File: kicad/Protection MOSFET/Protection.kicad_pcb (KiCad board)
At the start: 2 copper layers, 50 x 80 mm, 64 parts, among them P1 VI2, P2 LED, P3 VO2, P4 VI1, P5 VAC2, P6 VO1, P7 Taster, Q1 BC858, Q2 Q_NMOS_GDS, Q3 BC850, Q4 BC850, Q5 BC850, Q6 BC858, Q7 BC850, Q8 Q_NMOS_GDS, Q9 BC850, U1 LM319, U2 LTV-817

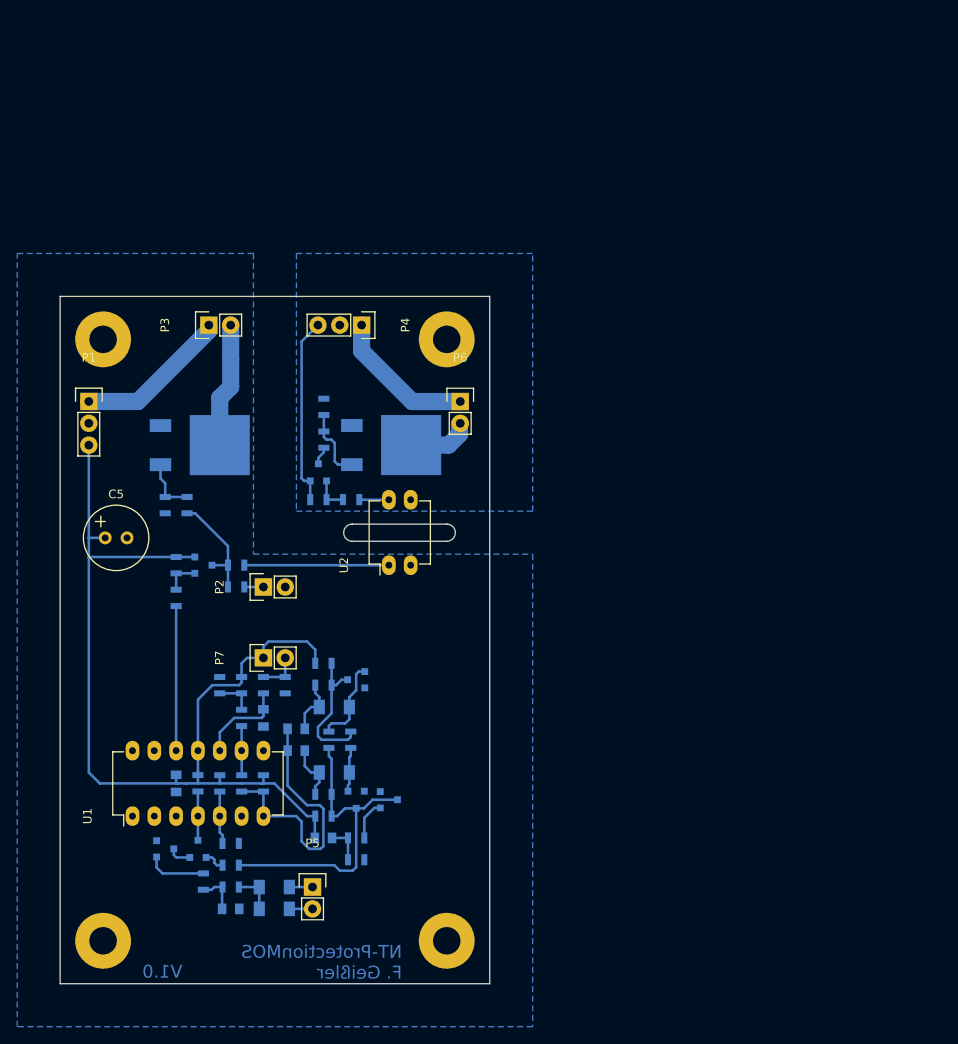
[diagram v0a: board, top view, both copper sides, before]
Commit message: Corrected MOSFET Protection board
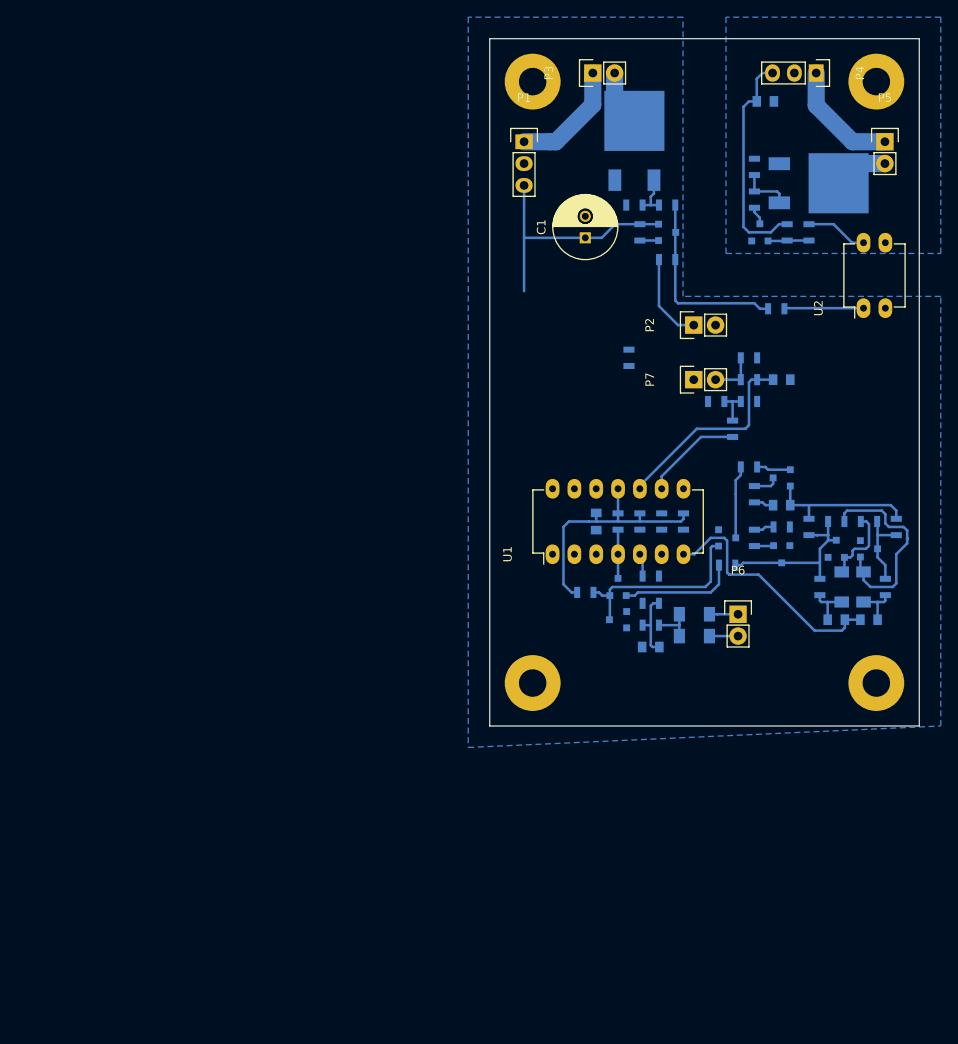
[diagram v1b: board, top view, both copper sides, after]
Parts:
- removed the REF** at (55.0, 125.0)
- removed the REF** at (95.0, 125.0)
- removed the REF** at (95.0, 55.0)
- removed the REF** at (55.0, 55.0)
- added C8: 1u, Capacitors_SMD:C_0805, B.Cu at (134.0, 59.7)
- added Q10: BC850, TO_SOT_Packages_SMD:SOT-23, B.Cu at (140.3, 79.4)
- added Q11: BC850, TO_SOT_Packages_SMD:SOT-23, B.Cu at (144.1, 79.4)
- added R32: 10k, Resistors_SMD:R_0805, B.Cu at (147.3, 76.8)
- added R33: 4k7, Resistors_SMD:R_0805, B.Cu at (130.2, 57.1)
- added R34: 47k, Resistors_SMD:R_0805, B.Cu at (146.1, 83.8)
- added REF**: Hole_M3, Mechanical:Hole_M3, F.Cu at (105.0, 95.0)
- added REF**: Hole_M3, Mechanical:Hole_M3, F.Cu at (145.0, 95.0)
- added REF**: Hole_M3, Mechanical:Hole_M3, F.Cu at (145.0, 25.0)
- added REF**: Hole_M3, Mechanical:Hole_M3, F.Cu at (105.0, 25.0)
- C1: value 15n -> 22u; footprint Capacitors_SMD:C_0805 -> Capacitors_ThroughHole:C_Radial_D7.5_L11.2_P2.5; moved to F.Cu
- C4: value 100n -> 15n
- C5: value 22u -> 100n; footprint Capacitors_Elko_ThroughHole:Elko_vert_11.2x7.5mm_RM2.5_CopperClear -> Capacitors_SMD:C_0805; moved to B.Cu
- C7: value 1u -> 100n
- P5: value VAC2 -> VO1
- P6: value VO1 -> VAC2
- Q1, Q3, Q4, Q9: footprint Housings_SOT-23_SOT-143_TSOT-6:SOT-23 -> TO_SOT_Packages_SMD:SOT-23
- Q2: footprint Transistors_SMD:sot428 -> TO_SOT_Packages_SMD:SOT-428
- Q5: value BC850 -> BC858; footprint Housings_SOT-23_SOT-143_TSOT-6:SOT-23 -> TO_SOT_Packages_SMD:SOT-23
- Q6: value BC858 -> BC850; footprint Housings_SOT-23_SOT-143_TSOT-6:SOT-23 -> TO_SOT_Packages_SMD:SOT-23
- Q7: value BC850 -> Q_NMOS_GDS; footprint Housings_SOT-23_SOT-143_TSOT-6:SOT-23 -> TO_SOT_Packages_SMD:SOT-428
- Q8: value Q_NMOS_GDS -> BC856; footprint Transistors_SMD:sot428 -> TO_SOT_Packages_SMD:SOT-23
- R10: value 47k -> 22k
- R11: value 2k2 -> 10k
- R12: value 100k -> 22k
- R13, R19, R2: value 22k -> 10k
- R14: value 10k -> 100
- R17: value 22k -> 1k
- R18: value 100 -> 100k
- R21: value 22k -> 47k
- R22: value 22k -> 120k
- R23, R25, R3, R30: value 10k -> 22k
- R24: value 47k -> 10k
- R26: value 120k -> 22k
- R31: value 4k7 -> 10k
- R4: value 22k -> 100
- R5: value 100 -> 22k
- R9: value 22k -> 2k2
- moved P5 109.4 mm to (146.0, 32.0)
- moved R15 103.6 mm to (130.8, 34.9), turned to 90 degrees
- moved C3 93.2 mm to (132.1, 27.3), turned to 180 degrees
- moved R9 90.7 mm to (133.3, 51.4), turned to 180 degrees
- moved R12 90.1 mm to (137.2, 42.5), turned to 270 degrees
- moved Q7 89.0 mm to (137.2, 36.8), turned to 90 degrees
- moved R14 87.6 mm to (130.8, 38.7), turned to 90 degrees
- moved C6 79.2 mm to (140.3, 87.6), turned to 180 degrees
- moved Q5 78.9 mm to (131.4, 42.5), turned to 180 degrees
- moved C1 76.2 mm to (111.1, 43.2), turned to 90 degrees
- moved R26 75.6 mm to (140.3, 76.2), turned to 180 degrees
- moved R11 74.9 mm to (134.6, 42.5), turned to 90 degrees
- moved D1 74.7 mm to (141.0, 83.8), turned to 90 degrees
- moved R4 73.2 mm to (120.7, 39.4), turned to 180 degrees
- moved R30 73.0 mm to (144.1, 76.2), turned to 180 degrees
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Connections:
- C1 pad 1: Net-(C1-Pad1) -> V+
- C1 pad 2: V+ -> V-
- C2 pad 2: Net-(C2-Pad2) -> V+
- C3 pad 1: Net-(C3-Pad1) -> /V-1
- C3 pad 2: Net-(C3-Pad2) -> /V+1
- C4 pad 1: Net-(C3-Pad1) -> Net-(C4-Pad1)
- C4 pad 2: Net-(C4-Pad2) -> V+
- C5 pad 1: V+ -> V-
- C5 pad 2: V- -> Net-(C5-Pad2)
- C6 pad 1: V- -> /BTN
- C6 pad 2: V+ -> Net-(C6-Pad2)
- C7 pad 1: V- -> Net-(C7-Pad1)
- C7 pad 2: Net-(C7-Pad2) -> /BTN
- D1 pad 1: Net-(D1-Pad1) -> Net-(C6-Pad2)
- D2 pad 1: Net-(D1-Pad1) -> Net-(D2-Pad1)
- D3 pad 1: Net-(C3-Pad2) -> Net-(D2-Pad1)
- D4 pad 1: Net-(C4-Pad2) -> Net-(C7-Pad1)
- P5 pad 1: Net-(D1-Pad2) -> Net-(P4-Pad1)
- P5 pad 2: Net-(D2-Pad2) -> Net-(P5-Pad2)
- P6 pad 1: Net-(P4-Pad1) -> Net-(D2-Pad2)
- P6 pad 2: Net-(P6-Pad2) -> Net-(D3-Pad2)
- Q3 pad 2: Net-(Q3-Pad2) -> /STARTUP_FB
- Q4 pad 1: Net-(Q4-Pad1) -> /MAINS_DET
- Q4 pad 3: Net-(Q3-Pad2) -> /STARTUP_FB
- Q5 pad 2: V- -> /V+1
- Q6 pad 1: Net-(Q6-Pad1) -> /STARTUP_FB
- Q6 pad 2: /V+1 -> V-
- Q7 pad 1: Net-(D3-Pad2) -> Net-(Q7-Pad1)
- Q7 pad 2: V- -> Net-(P5-Pad2)
- Q7 pad 3: Net-(Q5-Pad3) -> /V-1
- Q8 pad 2: Net-(P6-Pad2) -> V+
- Q8 pad 3: /V-1 -> Net-(Q8-Pad3)
- Q9 pad 1: Net-(D4-Pad2) -> Net-(Q9-Pad1)
- Q9 pad 3: Net-(Q9-Pad3) -> /FF_STARTUP
- R10 pad 1: Net-(C3-Pad2) -> Net-(Q3-Pad1)
- R10 pad 2: Net-(Q5-Pad3) -> /FF_STARTUP
- R11 pad 1: Net-(R11-Pad1) -> Net-(Q5-Pad1)
- R11 pad 2: /ON -> /V+1
- R12 pad 1: Net-(C1-Pad1) -> Net-(R12-Pad1)
- R12 pad 2: V- -> Net-(Q5-Pad1)
- R13 pad 1: Net-(C2-Pad2) -> /STARTUP_FB
- R13 pad 2: Net-(Q4-Pad1) -> V+
- R14 pad 1: Net-(C1-Pad1) -> Net-(Q5-Pad3)
- R14 pad 2: Net-(Q5-Pad1) -> Net-(Q7-Pad1)
- R15 pad 1: Net-(D1-Pad1) -> Net-(Q7-Pad1)
- R15 pad 2: Net-(C2-Pad2) -> /V-1
- R16 pad 1: Net-(Q6-Pad1) -> Net-(Q6-Pad3)
- R16 pad 2: /V+1 -> Net-(Q8-Pad1)
- R17 pad 1: Net-(R17-Pad1) -> Net-(Q8-Pad3)
- R17 pad 2: Net-(Q6-Pad1) -> Net-(C4-Pad1)
- R18 pad 1: Net-(Q6-Pad3) -> Net-(C4-Pad1)
- R18 pad 2: Net-(Q8-Pad1) -> V-
- R19 pad 1: Net-(Q8-Pad1) -> Net-(C4-Pad1)
- R19 pad 2: /V-1 -> Net-(Q9-Pad1)
- R2 pad 1: V- -> Net-(Q1-Pad1)
- R2 pad 2: Net-(Q2-Pad1) -> V+
- R20 pad 1: V+ -> /BTN
- R20 pad 2: Net-(Q5-Pad3) -> V+
- R21 pad 1: Net-(D4-Pad2) -> Net-(C6-Pad2)
- R21 pad 2: Net-(Q5-Pad3) -> /FF_STARTUP
- R22 pad 1: Net-(Q9-Pad3) -> Net-(R22-Pad1)
- R22 pad 2: Net-(D3-Pad2) -> /BTN
- R23 pad 1: V+ -> Net-(C5-Pad2)
- R23 pad 2: Net-(Q9-Pad3) -> /MAINS_DET
- R24 pad 1: Net-(C4-Pad2) -> V+
- R24 pad 2: Net-(Q9-Pad3) -> /FF_STARTUP
- R25 pad 1: Net-(C3-Pad1) -> Net-(D2-Pad1)
- R25 pad 2: V+ -> Net-(C5-Pad2)
- R26 pad 1: Net-(R26-Pad1) -> Net-(D4-Pad2)
- R26 pad 2: Net-(C3-Pad1) -> /FF_STARTUP
- R27 pad 2: Net-(R26-Pad1) -> Net-(R22-Pad1)
- R3 pad 1: Net-(Q1-Pad1) -> Net-(R3-Pad1)
- R3 pad 2: V+ -> Net-(Q1-Pad1)
- R30 pad 1: Net-(P7-Pad2) -> Net-(Q11-Pad3)
- R30 pad 2: Net-(C7-Pad2) -> Net-(D1-Pad2)
- R31 pad 1: V- -> Net-(P7-Pad2)
- R31 pad 2: Net-(P7-Pad2) -> Net-(C8-Pad2)
- R4 pad 1: Net-(R4-Pad1) -> /ON
- R4 pad 2: Net-(Q1-Pad1) -> Net-(Q2-Pad1)
- R5 pad 2: /ON -> V-
- R9 pad 1: Net-(Q3-Pad1) -> Net-(R9-Pad1)
- R9 pad 2: Net-(Q5-Pad3) -> /ON
- U1 pad 10: Net-(C7-Pad2) -> Net-(C8-Pad2)
- U1 pad 12: Net-(R4-Pad1) -> Net-(R3-Pad1)
- U1 pad 7: Net-(C3-Pad1) -> /BTN
- U1 pad 9: Net-(R26-Pad1) -> Net-(R22-Pad1)
- U2 pad 1: Net-(R11-Pad1) -> Net-(R9-Pad1)
- U2 pad 4: Net-(R17-Pad1) -> Net-(R12-Pad1)
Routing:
- net V+: track 117.3 -> 75.4 mm
- net Net-(Q5-Pad3): track 37.5 -> 2.12 mm
- net Net-(C3-Pad1): track 31.7 -> 0.00 mm
- net /BTN: track 0.00 -> 29.1 mm
- net Net-(C8-Pad2): track 0.00 -> 23.9 mm
- net /STARTUP_FB: track 0.00 -> 22.6 mm
- net /FF_STARTUP: track 0.00 -> 20.2 mm
- net Net-(R4-Pad1): track 16.8 -> 0.00 mm
- net Net-(R11-Pad1): track 16.8 -> 0.00 mm
- net Net-(Q9-Pad3): track 16.0 -> 0.00 mm
- net Net-(D4-Pad2): track 10.1 -> 24.0 mm
- net Net-(R22-Pad1): track 0.00 -> 11.6 mm
- net Net-(Q3-Pad1): track 2.49 -> 13.6 mm
- net Net-(C7-Pad2): track 10.6 -> 0.00 mm
- net /ON: track 13.0 -> 22.3 mm
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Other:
- outline, holes or cut-outs redrawn
- board text removed: "NT-ProtectionMOS F. Geißler"
- board text removed: "V1.0"
